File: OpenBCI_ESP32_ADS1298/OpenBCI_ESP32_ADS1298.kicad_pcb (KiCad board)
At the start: 6 copper layers, 50 x 50 mm, 75 parts, among them J1 Conn_02x13_Odd_Even, J2 Conn_02x08_Odd_Even, J3 Conn_02x03_Odd_Even, J4 Conn_02x02_Odd_Even, J5 Conn_01x02, J6 Conn_01x02, J7 Conn_01x02, U1 TPD4E1B06, U2 TPD4E1B06, U3 TPD4E1B06, U4 TPD4E1B06, U5 TPD4E1B06, U6 TPD4E1B06, U7 ADS1298RIZXGR

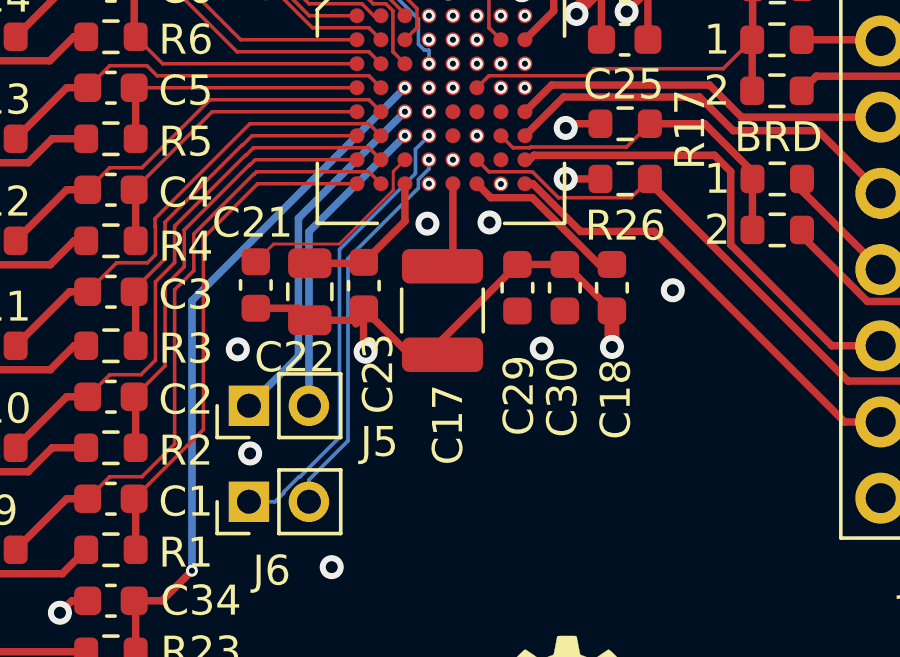
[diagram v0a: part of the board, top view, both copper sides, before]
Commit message: Update footprints
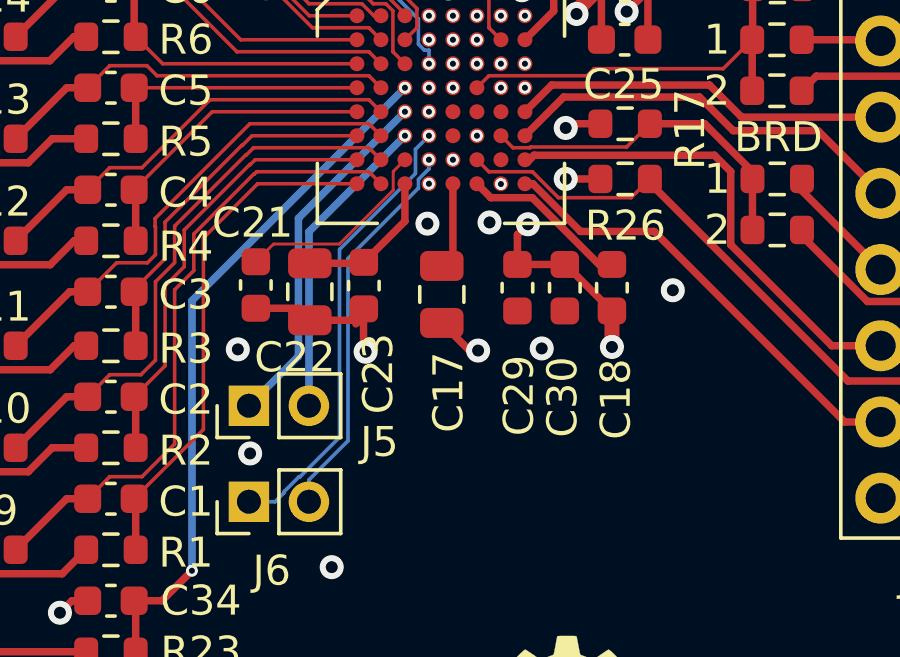
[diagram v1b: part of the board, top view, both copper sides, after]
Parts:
- C17: value 100u -> 22u; footprint Capacitor_SMD:C_1210_3225Metric -> Capacitor_SMD:C_0805_2012Metric
- moved C17 0.54 mm to (131.0, 80.5)
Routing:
- net -2V5: track 25.3 -> 21.1 mm, vias 12 -> 14
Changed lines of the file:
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@@
     )
   )
-  (footprint "Capacitor_SMD:C_1210_3225Metric" (layer "F.Cu")
-    (at 131.05 81.025 -90)
-    (descr "Capacitor SMD 1210 (3225 Metric), square (rectangular) end terminal, IPC_7351 nominal, (Body size source: IPC-SM-782 page 76, https://www.pcb-3d.com/wordpress/wp-content/uploads/ipc-sm-782a_amendment_1_and_2.pdf), generated with kicad-footprint-generator")
+  (footprint "Capacitor_SMD:C_0805_2012Metric" (layer "F.Cu")
+    (at 131.03 80.49 -90)
+    (descr "Capacitor SMD 0805 (2012 Metric), square (rectangular) end terminal, IPC_7351 nominal, (Body size source: IPC-SM-782 page 76, https://www.pcb-3d.com/wordpress/wp-content/uploads/ipc-sm-782a_amendment_1_and_2.pdf, https://docs.google.com/spreadsheets/d/1BsfQQcO9C6DZCsRaXUlFlo91Tg2WpOkGARC1WS5S8t0/edit?usp=sharing), generated with kicad-footprint-generator")
     (tags "capacitor")
     (property "Sheetfile" "ADS1298.kicad_sch")
@@
     (property "ki_keywords" "cap capacitor")
     (attr smd)
-    (fp_text reference "C17" (at 3.805 -0.19 90) (layer "F.SilkS")
+    (fp_text reference "C17" (at 3.26 -0.22 -90) (layer "F.SilkS")
         (effects (font (size 1 1) (thickness 0.15)))
     )
-    (fp_text value "100u" (at 0 2.3 90) (layer "F.Fab")
+    (fp_text value "22u" (at 0 1.68 -90) (layer "F.Fab")
         (effects (font (size 1 1) (thickness 0.15)))
     )
-    (fp_text user "${REFERENCE}" (at 0 0 90) (layer "F.Fab")
-        (effects (font (size 0.8 0.8) (thickness 0.12)))
+    (fp_text user "${REFERENCE}" (at 0 0 -90) (layer "F.Fab")
+        (effects (font (size 0.5 0.5) (thickness 0.08)))
     )
-    (fp_line (start -0.711252 -1.36) (end 0.711252 -1.36)
+    (fp_line (start -0.261252 -0.735) (end 0.261252 -0.735)
       (stroke (width 0.12) (type solid)) (layer "F.SilkS"))
-    (fp_line (start -0.711252 1.36) (end 0.711252 1.36)
+    (fp_line (start -0.261252 0.735) (end 0.261252 0.735)
       (stroke (width 0.12) (type solid)) (layer "F.SilkS"))
-    (fp_line (start -2.3 -1.6) (end 2.3 -1.6)
+    (fp_line (start -1.7 -0.98) (end 1.7 -0.98)
       (stroke (width 0.05) (type solid)) (layer "F.CrtYd"))
-    (fp_line (start -2.3 1.6) (end -2.3 -1.6)
+    (fp_line (start -1.7 0.98) (end -1.7 -0.98)
       (stroke (width 0.05) (type solid)) (layer "F.CrtYd"))
-    (fp_line (start 2.3 -1.6) (end 2.3 1.6)
+    (fp_line (start 1.7 -0.98) (end 1.7 0.98)
       (stroke (width 0.05) (type solid)) (layer "F.CrtYd"))
-    (fp_line (start 2.3 1.6) (end -2.3 1.6)
+    (fp_line (start 1.7 0.98) (end -1.7 0.98)
       (stroke (width 0.05) (type solid)) (layer "F.CrtYd"))
-    (fp_line (start -1.6 -1.25) (end 1.6 -1.25)
+    (fp_line (start -1 -0.625) (end 1 -0.625)
       (stroke (width 0.1) (type solid)) (layer "F.Fab"))
-    (fp_line (start -1.6 1.25) (end -1.6 -1.25)
+    (fp_line (start -1 0.625) (end -1 -0.625)
       (stroke (width 0.1) (type solid)) (layer "F.Fab"))
-    (fp_line (start 1.6 -1.25) (end 1.6 1.25)
+    (fp_line (start 1 -0.625) (end 1 0.625)
       (stroke (width 0.1) (type solid)) (layer "F.Fab"))
-    (fp_line (start 1.6 1.25) (end -1.6 1.25)
+    (fp_line (start 1 0.625) (end -1 0.625)
       (stroke (width 0.1) (type solid)) (layer "F.Fab"))
-    (pad "1" smd roundrect (at -1.475 0 270) (size 1.15 2.7) (layers "F.Cu" "F.Paste" "F.Mask") (roundrect_rratio 0.217391)
+    (pad "1" smd roundrect (at -0.95 0 270) (size 1 1.45) (layers "F.Cu" "F.Paste" "F.Mask") (roundrect_rratio 0.25)
       (net 37 "Net-(U7-VCAP1)") (pintype "passive"))
-    (pad "2" smd roundrect (at 1.475 0 270) (size 1.15 2.7) (layers "F.Cu" "F.Paste" "F.Mask") (roundrect_rratio 0.217391)
+    (pad "2" smd roundrect (at 0.95 0 270) (size 1 1.45) (layers "F.Cu" "F.Paste" "F.Mask") (roundrect_rratio 0.25)
       (net 2 "-2V5") (pintype "passive"))
-    (model "${KICAD6_3DMODEL_DIR}/Capacitor_SMD.3dshapes/C_1210_3225Metric.wrl"
+    (model "${KICAD6_3DMODEL_DIR}/Capacitor_SMD.3dshapes/C_0805_2012Metric.wrl"
       (offset (xyz 0 0 0))
       (scale (xyz 1 1 1))
@@
   (via (at 130.6 74.4) (size 0.4) (drill 0.2) (layers "F.Cu" "B.Cu") (net 1))
   (segment (start 128.42 82.33) (end 128.49 82.4) (width 0.25) (layer "F.Cu") (net 2))
+  (segment (start 133.55 78.5) (end 133.9 78.15) (width 0.25) (layer "F.Cu") (net 2))
+  (segment (start 133.55 78.61) (end 133.55 78.5) (width 0.25) (layer "F.Cu") (net 2))
   (segment (start 109.35 89.35) (end 109.2 89.2) (width 0.25) (layer "F.Cu") (net 2))
   (segment (start 133.31 68.185) (end 133.31 69.19) (width 0.25) (layer "F.Cu") (net 2))
-  (segment (start 129.96 82.5) (end 131.05 82.5) (width 0.25) (layer "F.Cu") (net 2))
+  (segment (start 131.95 82.36) (end 132.24 82.36) (width 0.25) (layer "F.Cu") (net 2))
   (segment (start 129.855 67.91) (end 130.74 68.795) (width 0.25) (layer "F.Cu") (net 2))
   (segment (start 133.015 67.89) (end 133.31 68.185) (width 0.25) (layer "F.Cu") (net 2))
@@
   (segment (start 126.23 80.95) (end 126.63 81.35) (width 0.25) (layer "F.Cu") (net 2))
   (segment (start 130.74 68.795) (end 130.74 69.18) (width 0.25) (layer "F.Cu") (net 2))
+  (segment (start 131.03 81.44) (end 131.95 82.36) (width 0.25) (layer "F.Cu") (net 2))
   (segment (start 133.015 66.19) (end 133.015 67.89) (width 0.25) (layer "F.Cu") (net 2))
-  (segment (start 131.05 81.99) (end 133.55 79.49) (width 0.25) (layer "F.Cu") (net 2))
-  (segment (start 128.43 80.97) (end 129.96 82.5) (width 0.25) (layer "F.Cu") (net 2))
   (segment (start 136.7 81.04) (end 136.7 82.24) (width 0.5) (layer "F.Cu") (net 2))
   (segment (start 110.05 89.35) (end 109.35 89.35) (width 0.25) (layer "F.Cu") (net 2))
@@
   (segment (start 128.05 81.35) (end 128.43 80.97) (width 0.25) (layer "F.Cu") (net 2))
   (segment (start 128.42 80.98) (end 128.42 82.33) (width 0.25) (layer "F.Cu") (net 2))
-  (segment (start 131.05 82.5) (end 131.05 81.99) (width 0.25) (layer "F.Cu") (net 2))
+  (segment (start 133.55 79.49) (end 133.55 78.61) (width 0.25) (layer "F.Cu") (net 2))
   (segment (start 135.13 79.49) (end 133.55 79.49) (width 0.25) (layer "F.Cu") (net 2))
   (segment (start 129.845 66.18) (end 129.845 67.9) (width 0.25) (layer "F.Cu") (net 2))
@@
   (via (at 131.4 72.8) (size 0.4) (drill 0.2) (layers "F.Cu" "B.Cu") (net 2))
   (via (at 130.74 69.18) (size 0.8) (drill 0.4) (layers "F.Cu" "B.Cu") (net 2))
+  (via (at 133.9 78.15) (size 0.8) (drill 0.4) (layers "F.Cu" "B.Cu") (net 2))
   (via (at 130.6 73.6) (size 0.4) (drill 0.2) (layers "F.Cu" "B.Cu") (net 2))
   (via (at 131.4 73.6) (size 0.4) (drill 0.2) (layers "F.Cu" "B.Cu") (net 2))
+  (via (at 132.24 82.36) (size 0.8) (drill 0.4) (layers "F.Cu" "B.Cu") (net 2))
   (via (at 133.8 71.2) (size 0.4) (drill 0.2) (layers "F.Cu" "B.Cu") (net 2))
   (via (at 128.49 82.4) (size 0.8) (drill 0.4) (layers "F.Cu" "B.Cu") (net 2))
@@
   (segment (start 120.025 62.6) (end 119.225 63.4) (width 0.12) (layer "F.Cu") (net 36))
   (segment (start 118.525 63.4) (end 116.825 65.1) (width 0.25) (layer "F.Cu") (net 36))
-  (segment (start 131.4 76.8) (end 131.4 79.2) (width 0.25) (layer "F.Cu") (net 37))
-  (segment (start 131.4 79.2) (end 131.05 79.55) (width 0.25) (layer "F.Cu") (net 37))
+  (segment (start 131.4 76.8) (end 131.4 79.17) (width 0.25) (layer "F.Cu") (net 37))
+  (segment (start 131.4 79.17) (end 131.03 79.54) (width 0.25) (layer "F.Cu") (net 37))
   (segment (start 134.045 77.265) (end 136.27 79.49) (width 0.25) (layer "F.Cu") (net 38))
   (segment (start 136.27 79.49) (end 136.7 79.49) (width 0.25) (layer "F.Cu") (net 38))

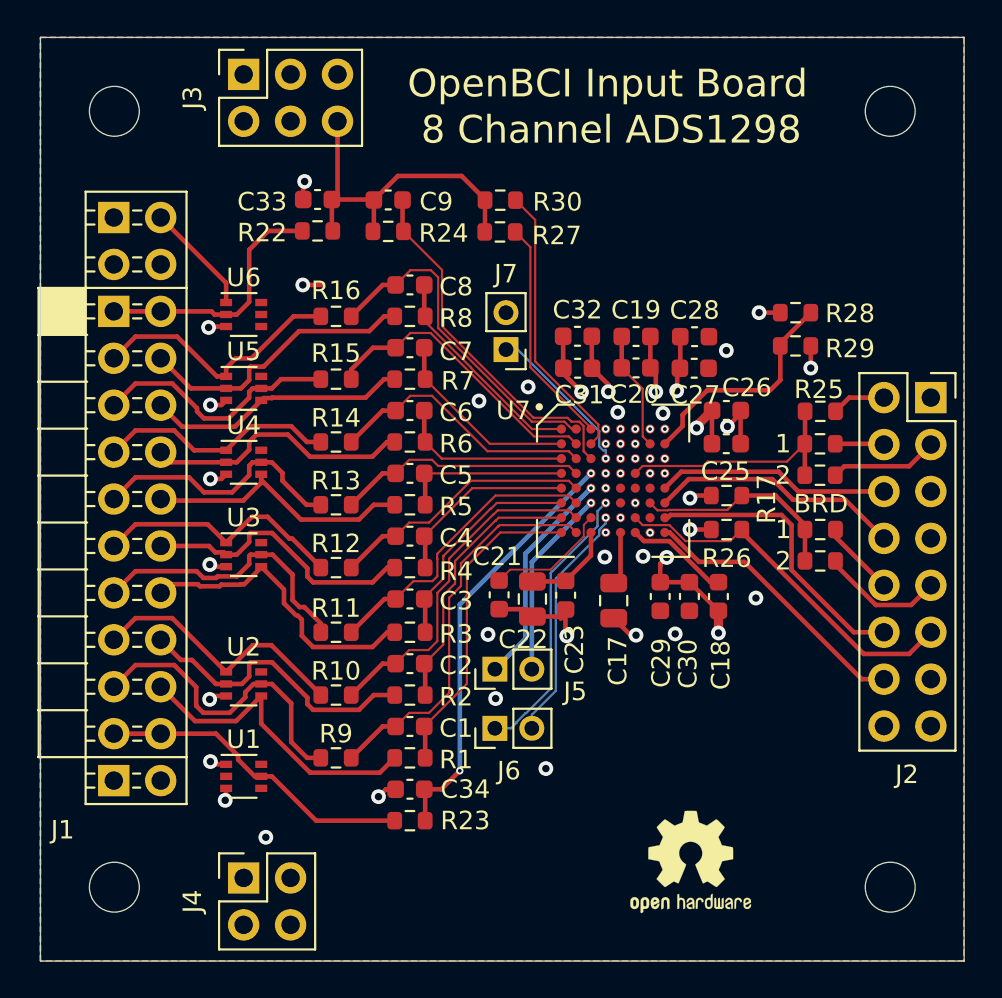
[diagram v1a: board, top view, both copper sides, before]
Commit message: Changes to meet JLCPCB Rules
Change BGA pad size and track routing. Change Via size to lower cost
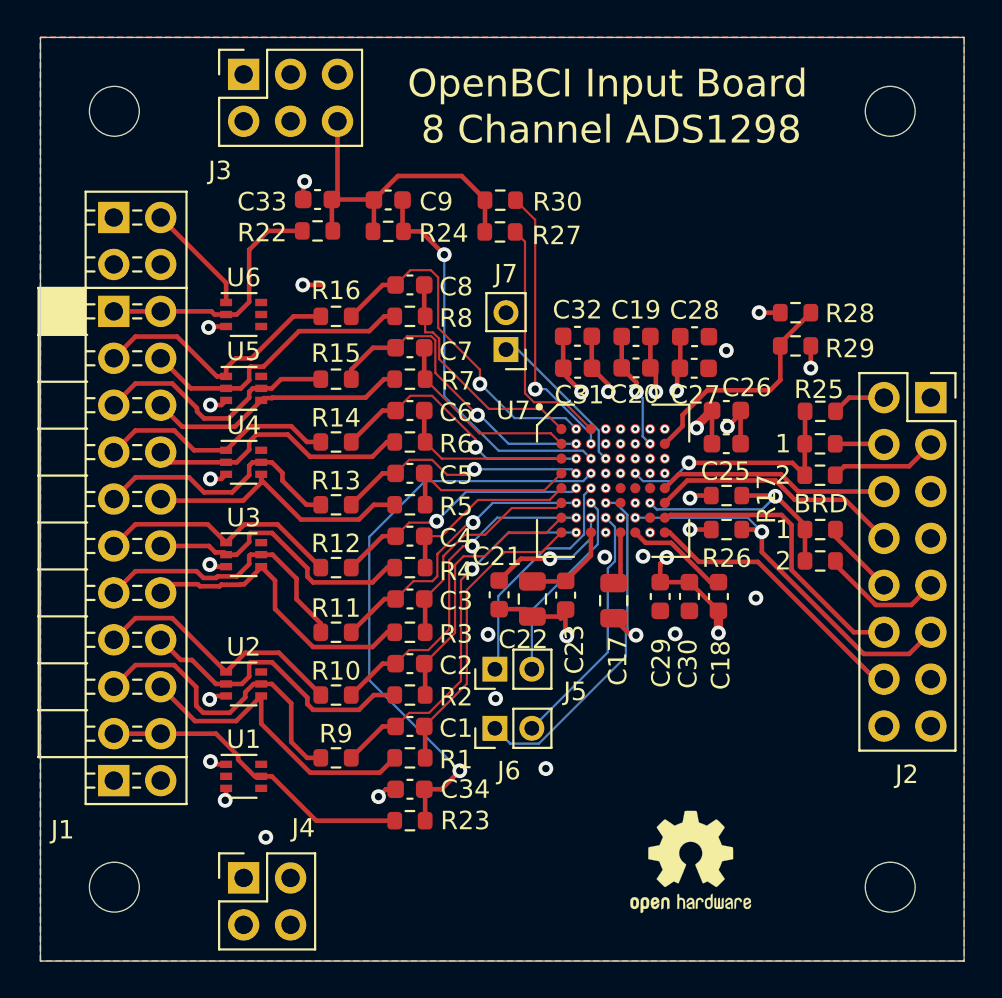
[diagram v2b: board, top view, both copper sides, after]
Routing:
- net /ADS1298/WCT: track 23.1 -> 32.2 mm
- net Net-(J6-Pin_1): track 15.2 -> 18.5 mm
- net Net-(U7-RLDINV): track 19.6 -> 21.5 mm, vias 0 -> 2
- net /ADS1298/CS: track 11.5 -> 13.2 mm, vias 0 -> 2
- net /ADS1298/RESET: track 20.1 -> 21.3 mm, vias 0 -> 2
- net /ADS1298/IN8P: track 11.7 -> 12.7 mm
- net Net-(U7-RLDIN): track 12.4 -> 13.3 mm
- net /ADS1298/IN7N: track 16.0 -> 16.9 mm, vias 0 -> 2
- net /ADS1298/IN1N: track 21.3 -> 20.4 mm, vias 0 -> 2
- net Net-(J5-Pin_1): track 12.0 -> 12.7 mm
- net /ADS1298/IN1P: track 17.2 -> 16.5 mm
- net /ADS1298/IN5P: track 9.15 -> 9.90 mm
- net /ADS1298/IN8N: track 18.4 -> 18.8 mm, vias 0 -> 2
- net /ADS1298/IN3N: track 16.1 -> 15.8 mm, vias 0 -> 2
- net /ADS1298/IN4N: track 14.3 -> 14.0 mm, vias 0 -> 2
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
